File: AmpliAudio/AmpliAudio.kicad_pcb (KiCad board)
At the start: 2 copper layers, 109.2 x 99.1 mm, 52 parts, among them J2 Conn_01x02, J3 Conn_01x03, Q1 2N2907, Q10 TIP32, Q11 BD138, Q12 TIP31, Q13 2N2222, Q2 2N2907, Q3 2N2907, Q4 2N2222, Q5 2N2222, Q6 2N2907, Q7 2N2907, Q8 BD139, Q9 BD139, U1 RelayCT, U2 Jack_Mono

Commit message: Routage partie 1
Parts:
- moved Dz1 214.4 mm to (30.5, 83.2), turned to 270 degrees
- moved Q3 209.6 mm to (34.5, 99.6), turned to 180 degrees
- moved C5 208.0 mm to (41.3, 81.3)
- moved R1 203.6 mm to (45.7, 112.3), turned to 270 degrees
- moved R5 200.0 mm to (35.6, 93.3), turned to 90 degrees
- moved Q2 184.5 mm to (39.6, 106.2), turned to 270 degrees
- moved Q1 180.1 mm to (55.4, 99.1)
- moved C4 177.7 mm to (30.5, 75.6)
- moved C2 174.9 mm to (87.6, 111.8)
- moved R4 173.3 mm to (41.3, 86.4)
- moved Q9 171.7 mm to (47.0, 69.8), turned to 180 degrees
- moved Q4 170.2 mm to (90.4, 101.6), turned to 270 degrees
- moved R9 170.1 mm to (41.1, 95.5)
- moved Q13 169.3 mm to (83.2, 59.7)
- moved Q8 169.2 mm to (71.1, 74.2), turned to 180 degrees
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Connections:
- J2 pad 1: Net-(J2-Pad1) -> GND
- J2 pad 2: GND -> Net-(J2-Pad2)
- J3 pad 1: +12V -> -12V
- J3 pad 3: -12V -> +12V
- U1 pad c1: Net-(R11-Pad2) -> Net-(J2-Pad2)
- U1 pad c2: Net-(J2-Pad1) -> Net-(R11-Pad2)
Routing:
- net GND: track 0.00 -> 366.0 mm
- net -12V: track 0.00 -> 278.7 mm
- net +12V: track 0.00 -> 191.6 mm
- net Net-(R11-Pad2): track 0.00 -> 77.3 mm
- net Net-(Q6-Pad3): track 0.00 -> 53.8 mm
- net Net-(C1-Pad1): track 0.00 -> 33.6 mm
- net Net-(Q1-Pad1): track 0.00 -> 31.5 mm
- net Net-(Q11-Pad1): track 0.00 -> 28.6 mm
- net Net-(Q3-Pad1): track 0.00 -> 25.1 mm
- net Net-(Q10-Pad2): track 0.00 -> 21.9 mm
- net Net-(Q8-Pad3): track 0.00 -> 21.0 mm
- net Net-(D2-Pad1): track 0.00 -> 16.6 mm
- net Net-(C3-Pad1): track 0.00 -> 16.6 mm
- net Net-(D1-Pad2): track 0.00 -> 14.2 mm
- net Net-(J2-Pad2): track 0.00 -> 13.1 mm
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
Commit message: Routage partie 2
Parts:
- moved Q6 24.3 mm to (79.8, 88.4)
- moved R3 23.4 mm to (73.0, 111.8), turned to 270 degrees
- moved Q7 18.8 mm to (70.1, 94.0), turned to 0 degrees
- moved C6 17.1 mm to (108.6, 80.0)
- moved C7 16.7 mm to (108.6, 87.6)
- moved RV1 14.8 mm to (70.1, 82.3), turned to 180 degrees
- moved R15 12.6 mm to (98.4, 91.9)
- moved R10 11.3 mm to (63.0, 96.5)
- moved C2 7.24 mm to (92.1, 106.0)
- moved R6 6.38 mm to (93.3, 111.8), turned to 270 degrees
- moved Q1 5.31 mm to (60.3, 101.0)
- moved Q4 5.24 mm to (94.5, 98.3)
- moved Q5 3.58 mm to (99.7, 111.8), turned to 90 degrees
- moved R14 2.57 mm to (101.0, 76.2)
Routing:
- net GND: track 366.0 -> 549.9 mm
- net Net-(C2-Pad2): track 0.00 -> 163.9 mm
- net Net-(Q2-Pad2): track 0.00 -> 102.8 mm, vias 0 -> 2
- net -12V: track 278.7 -> 225.8 mm
- net Net-(C2-Pad1): track 0.00 -> 42.8 mm
- net Net-(Q6-Pad3): track 53.8 -> 94.3 mm
- net Net-(Q6-Pad1): track 0.00 -> 29.7 mm
- net Net-(Q2-Pad3): track 11.7 -> 36.3 mm
- net Net-(R8-Pad1): track 0.00 -> 20.9 mm
- net Net-(C1-Pad1): track 33.6 -> 54.4 mm
- net Net-(Q7-Pad1): track 0.00 -> 19.3 mm
- net Net-(Q6-Pad2): track 0.00 -> 18.2 mm
- net Net-(Q4-Pad1): track 0.00 -> 17.3 mm
- net Net-(R10-Pad2): track 0.00 -> 9.10 mm
- net Net-(Q5-Pad1): track 0.00 -> 6.33 mm
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
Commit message: Routage termine v1
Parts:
- moved Q1 15.1 mm to (74.9, 104.8)
- moved R8 14.8 mm to (80.6, 83.2)
- moved R4 8.25 mm to (41.3, 94.6)
- moved R9 5.34 mm to (41.3, 90.2)
- moved R7 5.21 mm to (41.3, 85.7)
- moved Q2 2.05 mm to (40.6, 108.0), turned to 0 degrees
- moved C2 1.91 mm to (92.1, 104.1)
- moved Q4 1.78 mm to (94.5, 96.5)
- moved R10 0.81 mm to (63.5, 95.9)
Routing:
- net Net-(Q6-Pad3): track 94.3 -> 68.1 mm
- net Net-(C2-Pad2): track 163.9 -> 139.4 mm
- net Net-(R8-Pad1): track 20.9 -> 5.83 mm
- net Net-(C1-Pad1): track 54.4 -> 40.7 mm
- net Net-(Q1-Pad1): track 35.7 -> 48.2 mm
- net +12V: track 189.3 -> 176.8 mm
- net Net-(C2-Pad1): track 42.8 -> 30.8 mm
- net GND: track 549.9 -> 538.7 mm
- net Net-(Q3-Pad1): track 29.4 -> 19.4 mm
- net Net-(Q2-Pad2): track 102.8 -> 93.0 mm
- net Net-(Q2-Pad3): track 36.3 -> 32.3 mm
- net -12V: track 225.8 -> 222.1 mm
- net Net-(Q6-Pad2): track 18.2 -> 17.5 mm
- net Net-(Q7-Pad1): track 19.3 -> 20.0 mm
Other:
- board text added: "26-04-2020"
- board text added: "AmpliAudio"
- board text added: "Mikhin - Frances"

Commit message: Routage termine v2
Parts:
- moved Q5 30.4 mm to (91.4, 82.5), turned to 180 degrees
- moved R6 29.5 mm to (97.2, 82.5), turned to 90 degrees
- moved R15 22.6 mm to (81.9, 107.3)
- moved C7 14.8 mm to (98.4, 98.4)
- moved C6 13.5 mm to (98.4, 88.9)
- moved C2 9.09 mm to (83.8, 100.3), turned to 90 degrees
- moved Q4 5.92 mm to (91.4, 91.4), turned to 180 degrees
- moved R1 3.81 mm to (49.5, 112.3)
- moved Q3 3.51 mm to (36.8, 102.2)
- moved Q2 3.42 mm to (43.8, 109.2)
- moved C10 1.91 mm to (121.3, 40.6)
- moved R13 1.27 mm to (72.4, 42.5)
- moved Q1 1.27 mm to (74.9, 106.0)
- moved C5 0.64 mm to (41.3, 80.6)
- moved R17 0.13 mm to (90.9, 61.6)
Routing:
- net Net-(C2-Pad2): track 139.4 -> 72.9 mm
- net GND: track 538.7 -> 506.6 mm
- net -12V: track 222.1 -> 207.4 mm
- net Net-(Q2-Pad2): track 93.0 -> 83.9 mm, vias 2 -> 0
- net Net-(Q4-Pad1): track 16.9 -> 11.0 mm
- net Net-(C1-Pad1): track 40.7 -> 35.6 mm
- net Net-(Dz1-Pad2): track 10.8 -> 14.4 mm
- net Net-(Q1-Pad1): track 48.2 -> 44.7 mm
- net Net-(Q2-Pad3): track 32.3 -> 29.1 mm
- net Net-(Q8-Pad3): track 19.8 -> 17.2 mm
- net Net-(C2-Pad1): track 30.8 -> 28.8 mm
- net Net-(Q3-Pad1): track 19.4 -> 17.6 mm
- net Net-(D2-Pad1): track 16.6 -> 18.0 mm
- net Net-(R11-Pad2): track 71.3 -> 72.6 mm
- net Net-(Q6-Pad3): track 68.1 -> 66.8 mm
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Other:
- board text added: "Mikhin & Frances"
- board text removed: "Mikhin - Frances"

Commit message: Routage termine v3
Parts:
- moved Q12 3.81 mm to (111.8, 59.7)
- moved HS1 3.81 mm to (114.3, 55.9)
- moved Q6 2.01 mm to (78.1, 89.5), turned to 0 degrees
- moved Q2 1.80 mm to (42.5, 108.0)
- moved R8 1.27 mm to (80.6, 84.5)
- moved RV1 1.02 mm to (70.1, 81.3)
- moved R6 0.90 mm to (96.5, 83.2)
- moved R1 0.65 mm to (48.9, 112.4)
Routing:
- net Net-(R10-Pad2): track 8.67 -> 13.5 mm
- net Net-(Q6-Pad3): track 66.8 -> 62.9 mm
- net Net-(Q11-Pad2): track 6.98 -> 10.8 mm
- net Net-(Dz1-Pad2): track 14.4 -> 17.8 mm
- net +12V: track 177.2 -> 179.8 mm
- net Net-(Q2-Pad2): track 83.9 -> 86.3 mm
- net Net-(D2-Pad1): track 18.0 -> 19.6 mm
- net Net-(Q6-Pad1): track 29.4 -> 28.0 mm
- net Net-(Q1-Pad1): track 44.7 -> 43.7 mm
- net Net-(R8-Pad1): track 5.83 -> 6.78 mm
- net Net-(C2-Pad2): track 72.9 -> 72.0 mm
- net Net-(Q8-Pad3): track 17.2 -> 16.3 mm
- net Net-(Q2-Pad3): track 29.1 -> 29.9 mm
- net Net-(C1-Pad1): track 35.6 -> 36.3 mm
- net GND: track 506.6 -> 506.0 mm

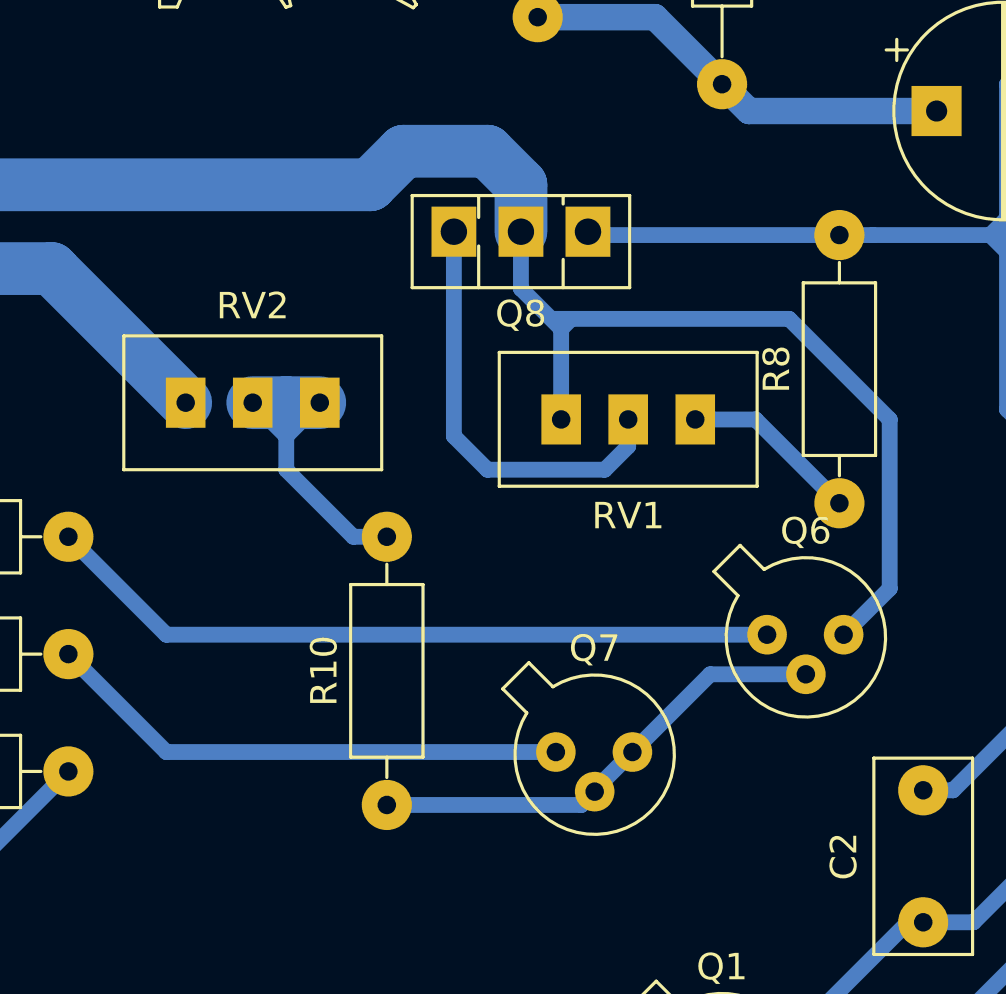
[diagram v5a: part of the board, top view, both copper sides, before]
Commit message: Correction inversion E/C des transistors
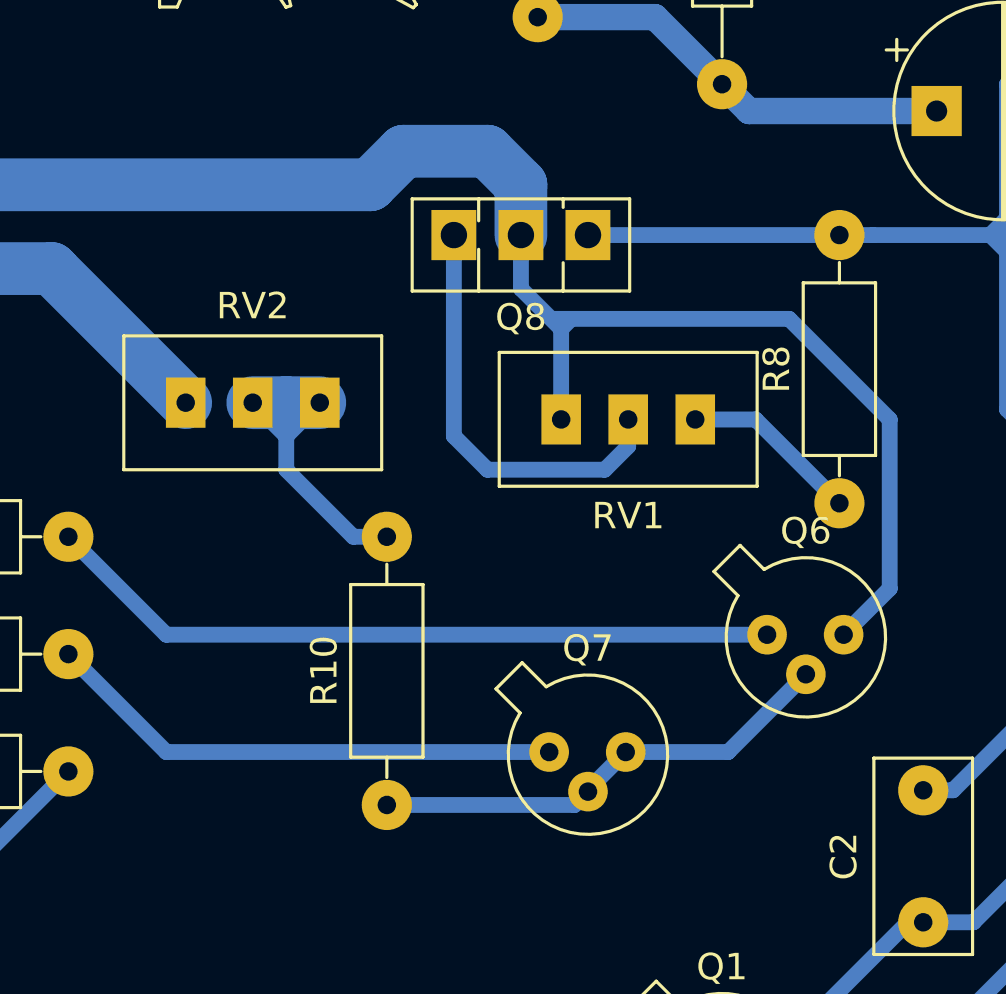
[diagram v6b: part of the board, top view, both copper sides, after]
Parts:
- moved Q7 0.25 mm to (69.8, 94.0)
- moved Q8 0.13 mm to (71.1, 74.3)
